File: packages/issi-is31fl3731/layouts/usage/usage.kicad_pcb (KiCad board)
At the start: 2 copper layers, 19 parts

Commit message: Clean PR: Only include packages from package-todos.md
- Updated layouts and parts for packages listed in package-todos.md only
- Includes adi-ad5693r, adi-adbms6822, adi-adbms6830, adi-adxl375, adi-ltc4316
- Updated ams-tsl2591, aosong-aht20, bosch sensors, diodes-inc, espressif
- Updated infineon, invensense, issi, liteon, macroblock, maxim components
- Updated memsic, microchip, rohm, nxp, opsco, st, ti, usb-connectors
- Renamed pjrc-teensy_4_1 to pjrc-teensy-4-1 (hyphen naming convention)
- Updated realtek-rtl8305nb

Removed 64+ packages that were not listed in package-todos.md to keep
PR focused only on packages that are being tracked for review.
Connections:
- net -anode-0 renamed channel_a[1]-anode
- net -anode-1 renamed channel_a[2]-anode
- net -anode-2 renamed channel_a[3]-anode
- net -anode-3 renamed channel_a[4]-anode
- net -anode-4 renamed channel_a[5]-anode
- net -anode-5 renamed channel_a[6]-anode
- net -anode-6 renamed channel_a[7]-anode
- net -anode-7 renamed channel_a[8]-anode
- net gnd renamed GND
- net hv renamed VCC

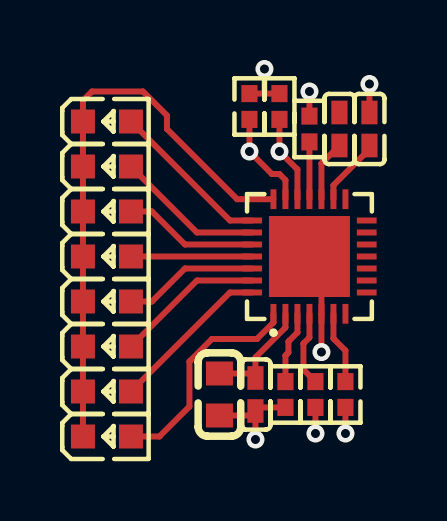
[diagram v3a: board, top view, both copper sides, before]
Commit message: issi-is31fl3731: package update to v0.2.0, ato:^0.14.0
Build targets:
  default = rc0
  usage = rc0
Package Verify: rc0
Version: 0.1.2 -> 0.2.0
Requires ato: ^0.14.0
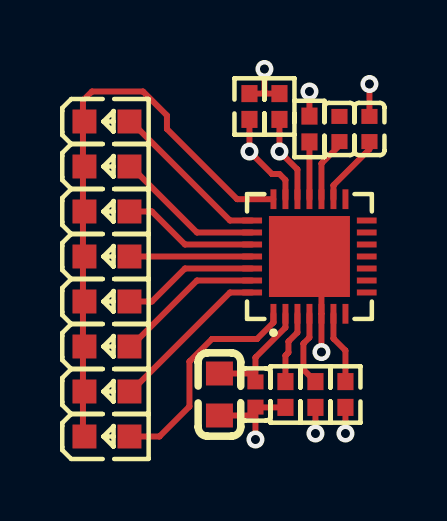
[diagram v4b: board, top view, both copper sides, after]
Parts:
- C1, C4, C5: value 100nF ±10% 16V X7R -> 1.0000000000000001e-07F
- C2: value 10µF ±20% 6.3V X5R -> 9.999999999999999e-06F
- R1: value 20kΩ ±1% 62.5mW -> 20000.0Ω
- R2, R3, R6: value 10kΩ ±1% 62.5mW -> 10000.0Ω
- R4, R5: value 10kΩ ±1% 62.5mW -> 4700.0Ω
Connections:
- net CB1 renamed 7
- net CB2 renamed 8
- net CB3 renamed 9
- net CB4 renamed 10
- net CB5 renamed 11
- net CB6 renamed 12
- net CB7 renamed 13
- net CB8 renamed 14
- net CB9 renamed 15
- net C_FILT renamed filter_capacitor-power-hv
- net GND renamed lv
- net IN renamed audio_input_capacitor-power-lv
- net VCC renamed hv
- net channel_a[1]-anode renamed anode
- net line renamed audio_input_capacitor-power-hv
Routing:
- net channel_a[8]-anode: track 7.49 -> 4.95 mm
- net channel_a[6]-anode: track 4.95 -> 7.49 mm
- net channel_a[5]-anode: track 4.50 -> 5.41 mm
- net anode: track 5.41 -> 4.50 mm

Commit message: remove all those other changes, just bosch baby
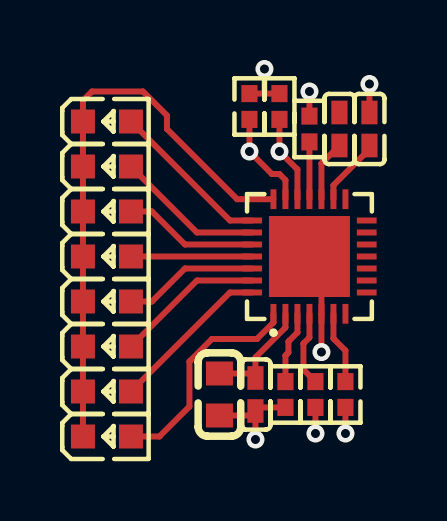
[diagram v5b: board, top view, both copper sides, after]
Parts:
- C1, C4, C5: value 1.0000000000000001e-07F -> 100nF ±10% 16V X7R
- C2: value 9.999999999999999e-06F -> 10µF ±20% 6.3V X5R
- R1: value 20000.0Ω -> 20kΩ ±1% 62.5mW
- R2, R3, R6: value 10000.0Ω -> 10kΩ ±1% 62.5mW
- R4, R5: value 4700.0Ω -> 10kΩ ±1% 62.5mW
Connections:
- net 10 renamed CB4
- net 11 renamed CB5
- net 12 renamed CB6
- net 13 renamed CB7
- net 14 renamed CB8
- net 15 renamed CB9
- net 7 renamed CB1
- net 8 renamed CB2
- net 9 renamed CB3
- net anode renamed channel_a[1]-anode
- net audio_input_capacitor-power-hv renamed line
- net audio_input_capacitor-power-lv renamed IN
- net filter_capacitor-power-hv renamed C_FILT
- net hv renamed VCC
- net lv renamed GND
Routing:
- net channel_a[8]-anode: track 4.95 -> 7.49 mm
- net channel_a[6]-anode: track 7.49 -> 4.95 mm
- net channel_a[5]-anode: track 5.41 -> 4.50 mm
- net channel_a[1]-anode: track 4.50 -> 5.41 mm

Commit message: fix some more packages
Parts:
- C1, C4, C5: value 100nF ±10% 16V X7R -> {8.99999998509884e-08..1.1000000014901162e-07}F
- C2: value 10µF ±20% 6.3V X5R -> {8.999999985098837e-06..1.1000000014901161e-05}F
- R1: value 20kΩ ±1% 62.5mW -> {20000.0±1.0%}Ω
- R2, R3, R6: value 10kΩ ±1% 62.5mW -> {10000.0±1.0%}Ω
- R4, R5: value 10kΩ ±1% 62.5mW -> {4700.0±1.0%}Ω
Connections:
- net CB1 renamed 7
- net CB2 renamed 8
- net CB3 renamed 9
- net CB4 renamed 10
- net CB5 renamed 11
- net CB6 renamed 12
- net CB7 renamed 13
- net CB8 renamed 14
- net CB9 renamed 15
- net GND renamed led_driver-power-lv
- net IN renamed audio_input_capacitor-power-lv
- net VCC renamed hv
- net line renamed audio_input-line
- D1 pad 2: channel_a[1]-anode -> anode
- D2 pad 2: channel_a[2]-anode -> anode
- D3 pad 2: channel_a[3]-anode -> anode
- D4 pad 2: channel_a[4]-anode -> anode
- D5 pad 2: channel_a[5]-anode -> anode
- D6 pad 2: channel_a[6]-anode -> anode
- D7 pad 2: channel_a[7]-anode -> anode
- D8 pad 2: channel_a[8]-anode -> anode
- U1 pad 1: channel_a[8]-anode -> channel_a[8]-line
- U1 pad 21: cathode -> channel_a[8]-line
- U1 pad 22: channel_a[1]-anode -> channel_a[8]-line
- U1 pad 23: channel_a[2]-anode -> channel_a[8]-line
- U1 pad 24: channel_a[3]-anode -> channel_a[8]-line
- U1 pad 25: channel_a[4]-anode -> channel_a[8]-line
- U1 pad 26: channel_a[5]-anode -> channel_a[8]-line
- U1 pad 27: channel_a[6]-anode -> channel_a[8]-line
- U1 pad 28: channel_a[7]-anode -> channel_a[8]-line
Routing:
- net channel_a[8]-anode: track 7.49 -> 0.00 mm
- net 29: track 0.00 -> 7.49 mm
- net channel_a[7]-anode: track 5.41 -> 0.00 mm
- net channel_a[1]-anode: track 5.41 -> 0.00 mm
- net 28: track 0.00 -> 5.41 mm
- net 25: track 0.00 -> 5.41 mm
- net channel_a[6]-anode: track 4.95 -> 0.00 mm
- net channel_a[2]-anode: track 4.95 -> 0.00 mm
- net 26: track 0.00 -> 4.95 mm
- net 23: track 0.00 -> 4.95 mm
- net channel_a[5]-anode: track 4.50 -> 0.00 mm
- net channel_a[3]-anode: track 4.50 -> 0.00 mm
- net 27: track 0.00 -> 4.50 mm
- net 22: track 0.00 -> 4.50 mm
- net channel_a[4]-anode: track 4.04 -> 0.00 mm
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
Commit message: fix issi-is31fl3731
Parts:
- C1, C4, C5: value {8.99999998509884e-08..1.1000000014901162e-07}F -> 1.0000000000000001e-07F
- C2: value {8.999999985098837e-06..1.1000000014901161e-05}F -> 9.999999999999999e-06F
- R1: value {20000.0±1.0%}Ω -> 20000.0Ω
- R2, R3, R6: value {10000.0±1.0%}Ω -> 10000.0Ω
- R4, R5: value {4700.0±1.0%}Ω -> 4700.0Ω
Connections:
- net C_FILT renamed filter_capacitor-power-hv
- net audio_input-line renamed audio_input_capacitor-power-hv
- net hv renamed led_driver-power-hv
- D1 pad 2: anode -> channel_a[1]-anode
- D2 pad 2: anode -> channel_a[2]-anode
- D3 pad 2: anode -> channel_a[3]-anode
- D4 pad 2: anode -> channel_a[4]-anode
- D5 pad 2: anode -> channel_a[5]-anode
- D6 pad 2: anode -> channel_a[6]-anode
- D7 pad 2: anode -> channel_a[7]-anode
- D8 pad 2: anode -> channel_a[8]-anode
- U1 pad 1: channel_a[8]-line -> channel_a[8]-anode
- U1 pad 21: channel_a[8]-line -> cathode
- U1 pad 22: channel_a[8]-line -> channel_a[1]-anode
- U1 pad 23: channel_a[8]-line -> channel_a[2]-anode
- U1 pad 24: channel_a[8]-line -> channel_a[3]-anode
- U1 pad 25: channel_a[8]-line -> channel_a[4]-anode
- U1 pad 26: channel_a[8]-line -> channel_a[5]-anode
- U1 pad 27: channel_a[8]-line -> channel_a[6]-anode
- U1 pad 28: channel_a[8]-line -> channel_a[7]-anode
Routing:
- net channel_a[6]-anode: track 0.00 -> 7.49 mm
- net 29: track 7.49 -> 0.00 mm
- net channel_a[7]-anode: track 0.00 -> 5.41 mm
- net channel_a[5]-anode: track 0.00 -> 5.41 mm
- net 28: track 5.41 -> 0.00 mm
- net 25: track 5.41 -> 0.00 mm
- net channel_a[8]-anode: track 0.00 -> 4.95 mm
- net channel_a[2]-anode: track 0.00 -> 4.95 mm
- net 26: track 4.95 -> 0.00 mm
- net 23: track 4.95 -> 0.00 mm
- net channel_a[4]-anode: track 0.00 -> 4.50 mm
- net channel_a[1]-anode: track 0.00 -> 4.50 mm
- net 27: track 4.50 -> 0.00 mm
- net 22: track 4.50 -> 0.00 mm
- net channel_a[3]-anode: track 0.00 -> 4.04 mm
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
